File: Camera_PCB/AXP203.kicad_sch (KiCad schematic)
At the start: 69 parts, among them J6 USB_C_Receptacle_PowerOnly_6P, SW1 PWR, SW2 RST, U1 AXP203

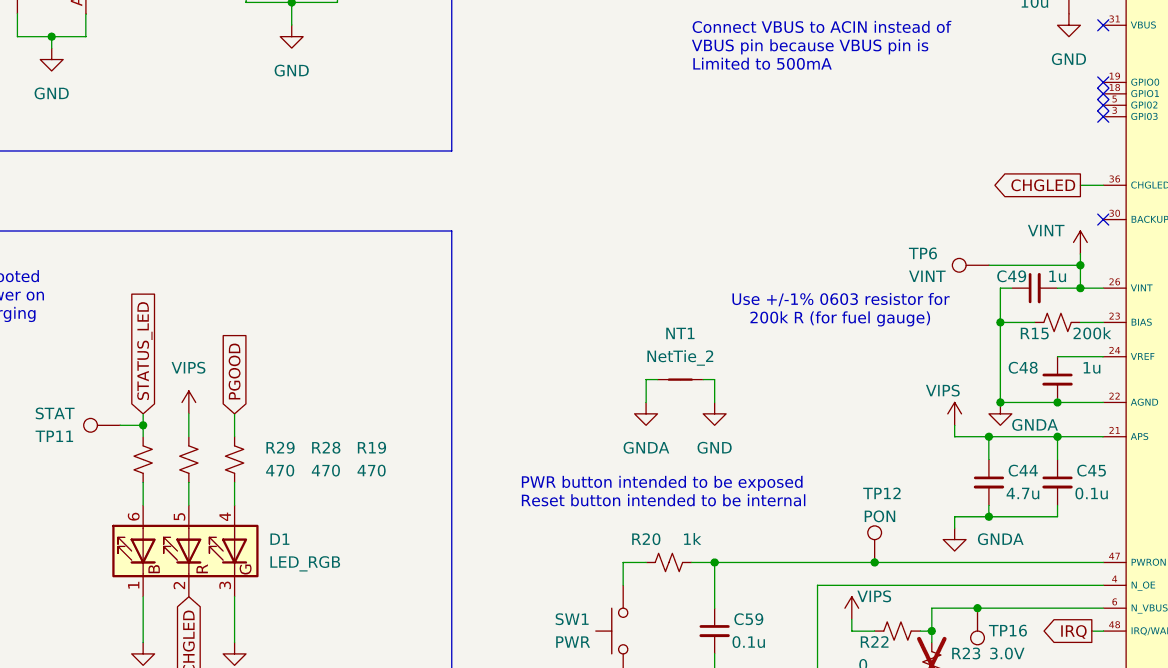
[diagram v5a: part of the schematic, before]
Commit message: Only unconnected grounds in schematic. Still need to thoroughly clean up.
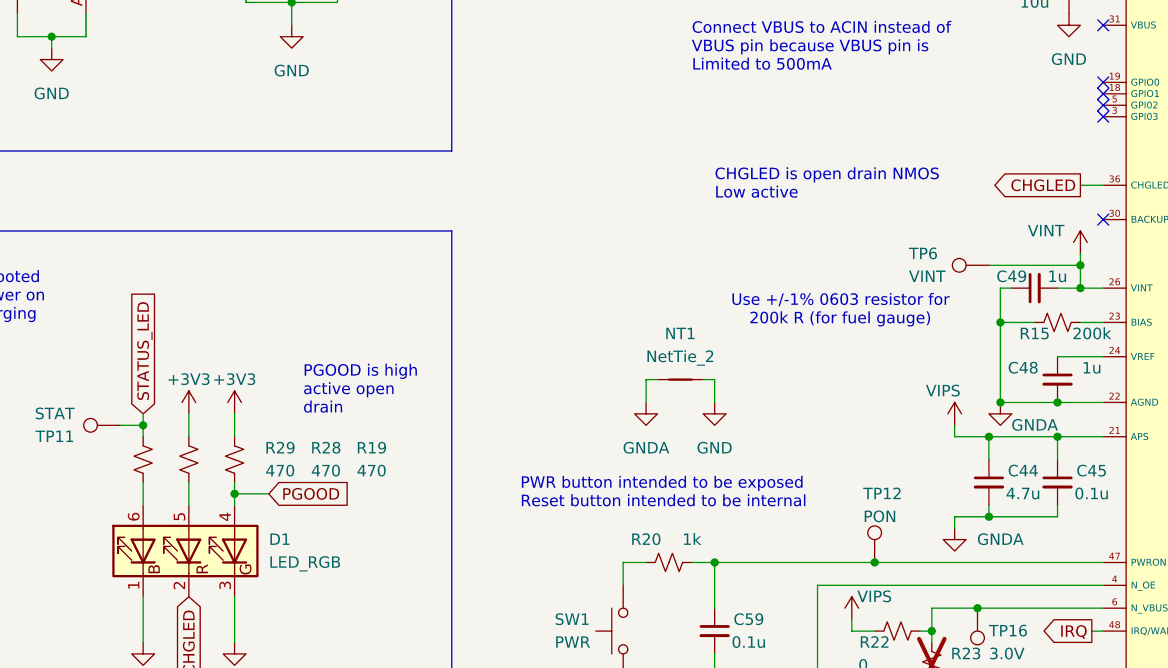
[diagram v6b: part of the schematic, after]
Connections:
- net +3V3: now also R19.1, R28.1
- net PGOOD: now also D1.4 (BA), R19.2; no longer R19.1
- net VIPS: no longer R28.1
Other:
- note added: "CHGLED is open drain NMOS Low active"
- note added: "PGOOD is high active open drain"
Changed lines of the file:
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@@
 		)
 	)
+	(text "PGOOD is high\nactive open\ndrain"
+		(exclude_from_sim no)
+		(at 67.31 109.22 0)
+		(effects
+			(font
+				(size 1.27 1.27)
+				(thickness 0.1588)
+			)
+			(justify left)
+		)
+	)
 	(text "Connect VBUS to ACIN instead of\nVBUS pin because VBUS pin is\nLimited to 500mA"
 		(exclude_from_sim no)
@@
 		)
 	)
+	(text "CHGLED is open drain NMOS\nLow active"
+		(exclude_from_sim no)
+		(at 113.03 86.36 0)
+		(effects
+			(font
+				(size 1.27 1.27)
+			)
+			(justify left)
+		)
+	)
 	(text "use 1nF caps as filter caps\nfor feedback pins\nplace close to IC"
 		(exclude_from_sim no)
@@
 	)
 	(junction
+		(at 59.69 120.65)
+		(diameter 0)
+		(color 0 0 0 0)
+	)
+	(junction
 		(at 143.51 123.19)
 		(diameter 0)
@@
 	(wire
 		(pts
+			(xy 59.69 120.65) (xy 63.5 120.65)
+		)
+		(stroke
+			(width 0)
+			(type default)
+		)
+	)
+	(wire
+		(pts
 			(xy 194.31 88.9) (xy 212.09 88.9)
 		)
@@
 	(wire
 		(pts
-			(xy 59.69 119.38) (xy 59.69 121.92)
+			(xy 59.69 119.38) (xy 59.69 120.65)
 		)
 		(stroke
@@
 	(wire
 		(pts
+			(xy 59.69 120.65) (xy 59.69 121.92)
+		)
+		(stroke
+			(width 0)
+			(type default)
+		)
+	)
+	(wire
+		(pts
 			(xy 219.71 95.25) (xy 219.71 96.52)
 		)
@@
 	)
 	(global_label "PGOOD"
-		(shape output)
-		(at 199.39 142.24 0)
+		(shape input)
+		(at 63.5 120.65 0)
 		(fields_autoplaced yes)
 		(effects
@@
 		)
 		(property "Intersheetrefs" "${INTERSHEET_REFS}"
-			(at 208.8462 142.24 0)
+			(at 72.9562 120.65 0)
 			(effects
 				(font
@@
 	)
 	(global_label "PGOOD"
-		(shape input)
-		(at 59.69 111.76 90)
+		(shape output)
+		(at 199.39 142.24 0)
 		(fields_autoplaced yes)
 		(effects
@@
 		)
 		(property "Intersheetrefs" "${INTERSHEET_REFS}"
-			(at 59.69 102.3038 90)
+			(at 208.8462 142.24 0)
 			(effects
 				(font
@@
 	)
 	(symbol
-		(lib_id "custom_chips:VIPS")
-		(at 54.61 111.76 0)
-		(mirror y)
-		(unit 1)
-		(exclude_from_sim no)
-		(in_bom yes)
-		(on_board yes)
-		(dnp no)
-		(property "Reference" "#PWR076"
-			(at 54.61 115.57 0)
-			(effects
-				(font
-					(size 1.27 1.27)
-				)
-				(hide yes)
-			)
-		)
-		(property "Value" "VIPS"
-			(at 54.61 106.68 0)
-			(effects
-				(font
-					(size 1.27 1.27)
-				)
-			)
-		)
-		(property "Footprint" ""
-			(at 54.61 111.76 0)
-			(effects
-				(font
-					(size 1.27 1.27)
-				)
-				(hide yes)
-			)
-		)
-		(property "Datasheet" ""
-			(at 54.61 111.76 0)
-			(effects
-				(font
-					(size 1.27 1.27)
-				)
-				(hide yes)
-			)
-		)
-		(property "Description" "Power symbol creates a global label with name \"VISP\""
-			(at 54.61 111.76 0)
-			(effects
-				(font
-					(size 1.27 1.27)
-				)
-				(hide yes)
-			)
-		)
-		(pin "1"
-		)
-		(instances
-			(project "CameraPCB"
-				(path "/400c1603-202c-4359-a830-d2f0d06dd3ce/63007821-20b4-4692-9a5a-85c4738356da"
-					(reference "#PWR076")
-					(unit 1)
-				)
-			)
-		)
-	)
-	(symbol
 		(lib_id "Device:R_Small_US")
 		(at 119.38 154.94 90)
@@
 	)
 	(symbol
+		(lib_id "power:+3V3")
+		(at 54.61 111.76 0)
+		(unit 1)
+		(exclude_from_sim no)
+		(in_bom yes)
+		(on_board yes)
+		(dnp no)
+		(property "Reference" "#PWR042"
+			(at 54.61 115.57 0)
+			(effects
+				(font
+					(size 1.27 1.27)
+				)
+				(hide yes)
+			)
+		)
+		(property "Value" "+3V3"
+			(at 54.61 107.95 0)
+			(effects
+				(font
+					(size 1.27 1.27)
+				)
+			)
+		)
+		(property "Footprint" ""
+			(at 54.61 111.76 0)
+			(effects
+				(font
+					(size 1.27 1.27)
+				)
+				(hide yes)
+			)
+		)
+		(property "Datasheet" ""
+			(at 54.61 111.76 0)
+			(effects
+				(font
+					(size 1.27 1.27)
+				)
+				(hide yes)
+			)
+		)
+		(property "Description" "Power symbol creates a global label with name \"+3V3\""
+			(at 54.61 111.76 0)
+			(effects
+				(font
+					(size 1.27 1.27)
+				)
+				(hide yes)
+			)
+		)
+		(pin "1"
+		)
+		(instances
+			(project "CameraPCB"
+				(path "/400c1603-202c-4359-a830-d2f0d06dd3ce/63007821-20b4-4692-9a5a-85c4738356da"
+					(reference "#PWR042")
+					(unit 1)
+				)
+			)
+		)
+	)
+	(symbol
 		(lib_id "custom_chips:VINT")
 		(at 153.67 93.98 0)
@@
 					(unit 1)
 				)
+			)
+		)
+	)
+	(symbol
+		(lib_id "power:+3V3")
+		(at 59.69 111.76 0)
+		(unit 1)
+		(exclude_from_sim no)
+		(in_bom yes)
+		(on_board yes)
+		(dnp no)
+		(property "Reference" "#PWR043"
+			(at 59.69 115.57 0)
+			(effects
+				(font
+					(size 1.27 1.27)
+				)
+				(hide yes)
+			)
+		)
+		(property "Value" "+3V3"
+			(at 59.69 107.95 0)
+			(effects
+				(font
+					(size 1.27 1.27)
+				)
+			)
+		)
+		(property "Footprint" ""
+			(at 59.69 111.76 0)
+			(effects
+				(font
+					(size 1.27 1.27)
+				)
+				(hide yes)
+			)
+		)
+		(property "Datasheet" ""
+			(at 59.69 111.76 0)
+			(effects
+				(font
+					(size 1.27 1.27)
+				)
+				(hide yes)
+			)
+		)
+		(property "Description" "Power symbol creates a global label with name \"+3V3\""
+			(at 59.69 111.76 0)
+			(effects
+				(font
+					(size 1.27 1.27)
+				)
+				(hide yes)
+			)
+		)
+		(pin "1"
+		)
+		(instances
+			(project "CameraPCB"
+				(path "/400c1603-202c-4359-a830-d2f0d06dd3ce/63007821-20b4-4692-9a5a-85c4738356da"
+					(reference "#PWR043")
+					(unit 1)
+				)

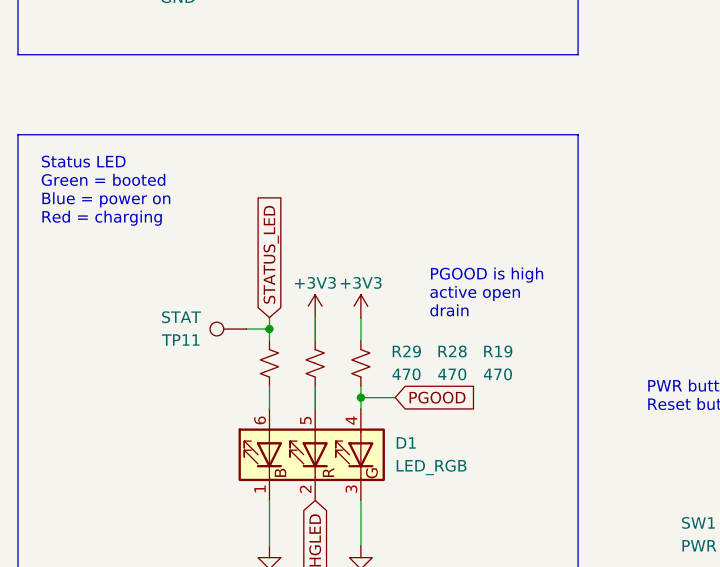
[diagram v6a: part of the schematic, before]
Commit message: PCB has no missing connections, (some missing grounds)
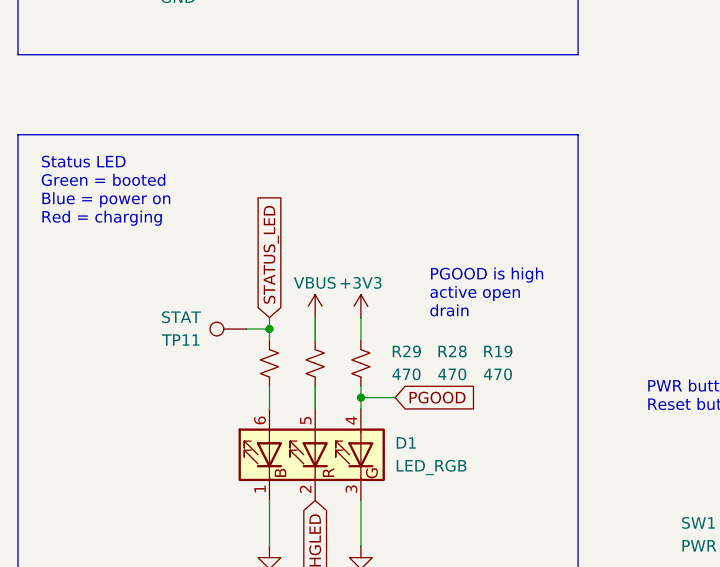
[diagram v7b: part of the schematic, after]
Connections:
- net +3V3: no longer R28.1
- net VBUS: now also R28.1
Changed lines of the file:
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@@
-	)
-	(symbol
-		(lib_id "power:+3V3")
-		(at 54.61 111.76 0)
-		(unit 1)
-		(exclude_from_sim no)
-		(in_bom yes)
-		(on_board yes)
-		(dnp no)
-		(property "Reference" "#PWR042"
-			(at 54.61 115.57 0)
-			(effects
-				(font
-					(size 1.27 1.27)
-				)
-				(hide yes)
-			)
-		)
-		(property "Value" "+3V3"
-			(at 54.61 107.95 0)
-			(effects
-				(font
-					(size 1.27 1.27)
-				)
-			)
-		)
-		(property "Footprint" ""
-			(at 54.61 111.76 0)
-			(effects
-				(font
-					(size 1.27 1.27)
-				)
-				(hide yes)
-			)
-		)
-		(property "Datasheet" ""
-			(at 54.61 111.76 0)
-			(effects
-				(font
-					(size 1.27 1.27)
-				)
-				(hide yes)
-			)
-		)
-		(property "Description" "Power symbol creates a global label with name \"+3V3\""
-			(at 54.61 111.76 0)
-			(effects
-				(font
-					(size 1.27 1.27)
-				)
-				(hide yes)
-			)
-		)
-		(pin "1"
-		)
-		(instances
-			(project "CameraPCB"
-				(path "/400c1603-202c-4359-a830-d2f0d06dd3ce/63007821-20b4-4692-9a5a-85c4738356da"
-					(reference "#PWR042")
-					(unit 1)
-				)
-			)
-		)
 	)
 	(symbol
@@
 					(unit 1)
 				)
+			)
+		)
+	)
+	(symbol
+		(lib_id "power:VBUS")
+		(at 54.61 111.76 0)
+		(unit 1)
+		(exclude_from_sim no)
+		(in_bom yes)
+		(on_board yes)
+		(dnp no)
+		(property "Reference" "#PWR042"
+			(at 54.61 115.57 0)
+			(effects
+				(font
+					(size 1.27 1.27)
+				)
+				(hide yes)
+			)
+		)
+		(property "Value" "VBUS"
+			(at 54.61 107.95 0)
+			(effects
+				(font
+					(size 1.27 1.27)
+				)
+			)
+		)
+		(property "Footprint" ""
+			(at 54.61 111.76 0)
+			(effects
+				(font
+					(size 1.27 1.27)
+				)
+				(hide yes)
+			)
+		)
+		(property "Datasheet" ""
+			(at 54.61 111.76 0)
+			(effects
+				(font
+					(size 1.27 1.27)
+				)
+				(hide yes)
+			)
+		)
+		(property "Description" "Power symbol creates a global label with name \"VBUS\""
+			(at 54.61 111.76 0)
+			(effects
+				(font
+					(size 1.27 1.27)
+				)
+				(hide yes)
+			)
+		)
+		(pin "1"
+		)
+		(instances
+			(project "CameraPCB"
+				(path "/400c1603-202c-4359-a830-d2f0d06dd3ce/63007821-20b4-4692-9a5a-85c4738356da"
+					(reference "#PWR042")
+					(unit 1)
+				)

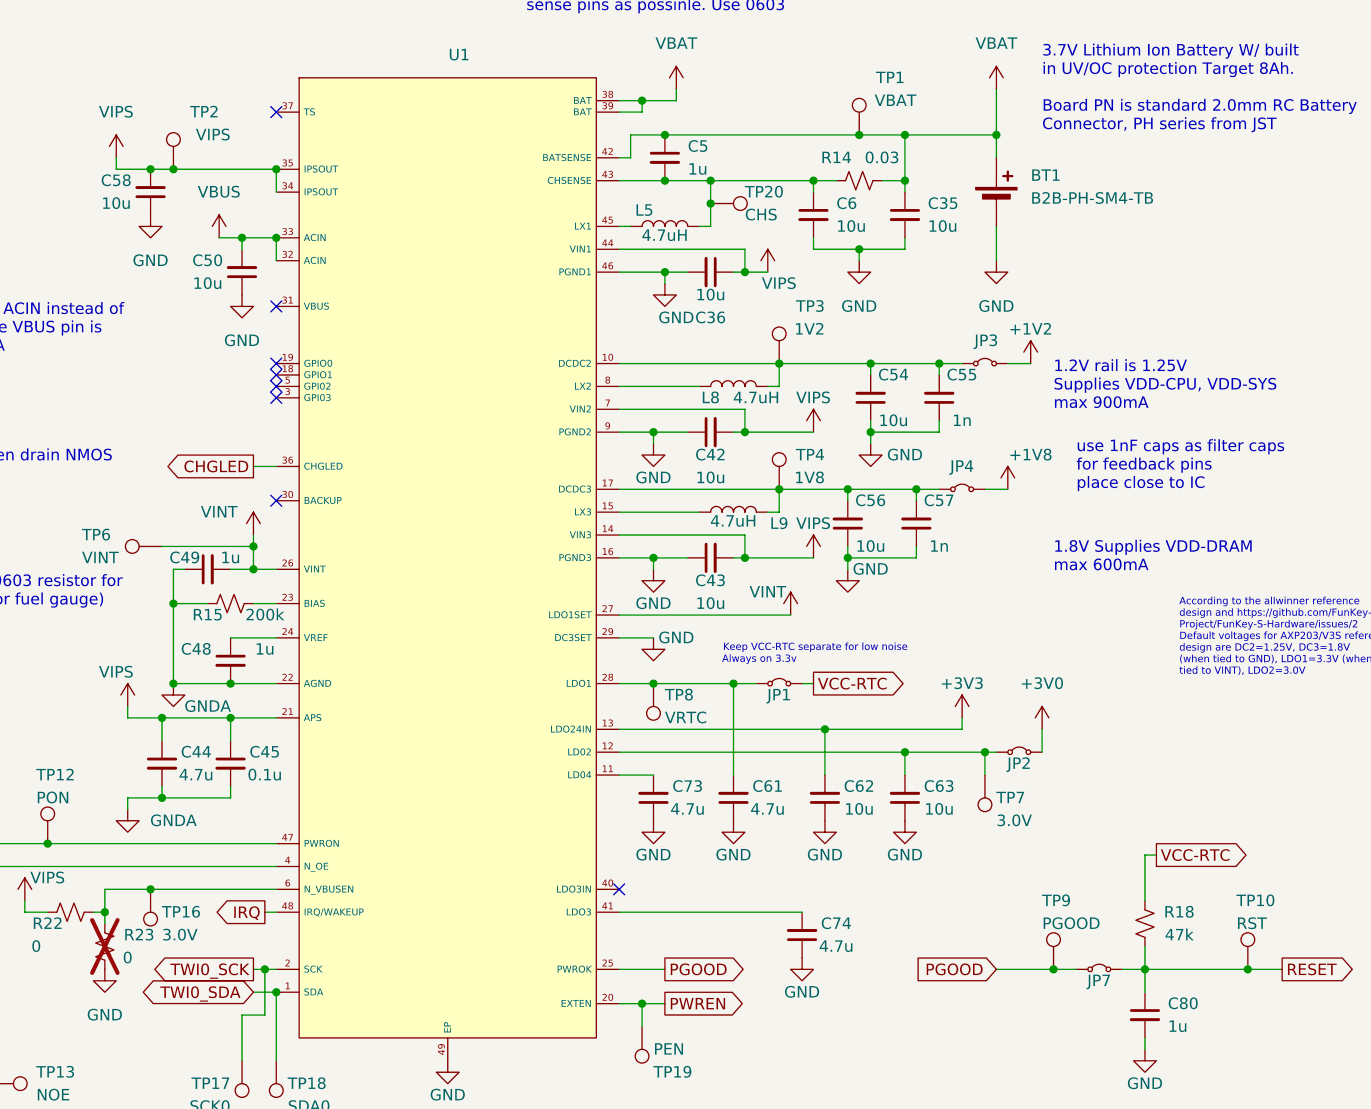
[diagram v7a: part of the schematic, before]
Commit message: Added 3d models, completed layout. Should still review more.
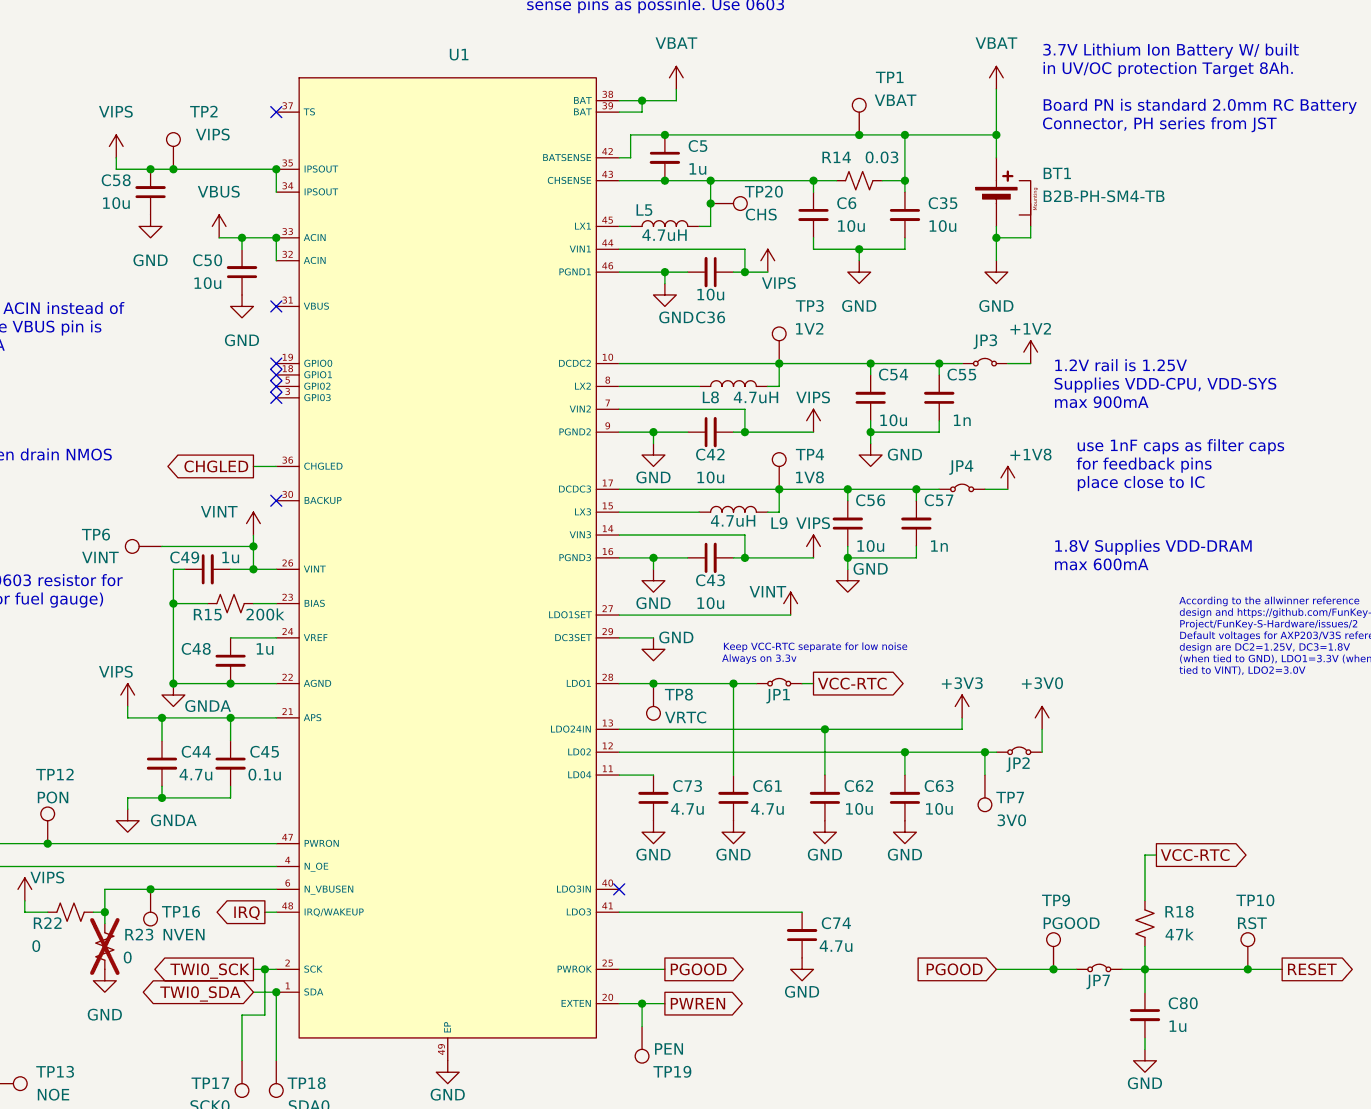
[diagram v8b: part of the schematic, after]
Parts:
- TP16: value 3.0V -> NVEN
- TP7: value 3.0V -> 3V0
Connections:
- net GND: now also BT1.MP
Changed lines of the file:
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@@
 	)
 	(junction
+		(at 236.22 60.96)
+		(diameter 0)
+		(color 0 0 0 0)
+	)
+	(junction
 		(at 226.06 118.11)
 		(diameter 0)
@@
 	(wire
 		(pts
+			(xy 240.03 59.69) (xy 240.03 60.96)
+		)
+		(stroke
+			(width 0)
+			(type default)
+		)
+	)
+	(wire
+		(pts
 			(xy 154.94 147.32) (xy 154.94 142.24)
 		)
@@
 	(wire
 		(pts
-			(xy 236.22 63.5) (xy 236.22 59.69)
+			(xy 236.22 63.5) (xy 236.22 60.96)
 		)
 		(stroke
@@
 	(wire
 		(pts
+			(xy 240.03 60.96) (xy 236.22 60.96)
+		)
+		(stroke
+			(width 0)
+			(type default)
+		)
+	)
+	(wire
+		(pts
 			(xy 204.47 59.69) (xy 204.47 57.15)
 		)
@@
 	(wire
 		(pts
+			(xy 236.22 60.96) (xy 236.22 59.69)
+		)
+		(stroke
+			(width 0)
+			(type default)
+		)
+	)
+	(wire
+		(pts
 			(xy 54.61 119.38) (xy 54.61 121.92)
 		)
@@
 			)
 		)
-		(property "Value" "3.0V"
+		(property "Value" "NVEN"
 			(at 143.51 138.43 0)
 			(effects
@@
 			)
 		)
-		(property "Value" "3.0V"
+		(property "Value" "3V0"
 			(at 236.22 125.73 0)
 			(effects
@@
 		(fields_autoplaced yes)
 		(property "Reference" "BT1"
-			(at 240.03 54.0384 0)
+			(at 241.3 53.848 0)
 			(effects
 				(font
@@
 		)
 		(property "Value" "B2B-PH-SM4-TB"
-			(at 240.03 56.5784 0)
+			(at 241.3 56.388 0)
 			(effects
 				(font
@@
 			)
 		)
-		(property "Datasheet" "~"
+		(property "Datasheet" "https://www.jst-mfg.com/product/pdf/eng/ePH.pdf"
 			(at 236.22 55.626 90)
 			(effects
@@
 		(pin "1"
 		)
+		(pin "MP"
+		)
 		(instances
